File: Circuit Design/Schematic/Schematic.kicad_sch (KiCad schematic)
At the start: 18 parts, among them U1 ESP32-WROOM-32

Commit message: Add files via upload
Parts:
- added Display: Conn_01x04_Female, Connector_PinSocket_2.54mm:PinSocket_1x04_P2.54mm_Vertical, symbol Connector:Conn_01x04_Female
- added Display_: Conn_01x14_Female, Connector_PinSocket_2.54mm:PinSocket_1x14_P2.54mm_Vertical, symbol Connector:Conn_01x14_Female
- added Pull_Down_Miso_Res: 10k, symbol Device:R
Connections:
- net 3v3: now also Display_.14 (Pin_14), Display_.7 (Pin_7)
- net GND: now also Display_.13 (Pin_13), Pull_Down_Miso_Res.2
- net MISO: now also Display_.6 (Pin_6), Pull_Down_Miso_Res.1
- net MOSI: now also Display_.9 (Pin_9)
- net Rst_2: now also U1.12 (IO27); no longer U1.23 (IO15)
- net SCK: now also Display_.8 (Pin_8)
- net IO13: now reaches R_prog.2, U1.16 (IO13)
- net Rst_D: now reaches U1.6 (IO34)
- net Rst_D: now also Display_.11 (Pin_11)
- net D/C: now reaches U1.7 (IO35)
- net D/C: now also Display_.10 (Pin_10)
- new net CS_Display: Display_.12 (Pin_12), U1.23 (IO15)
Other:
- note added: "Display"
- moved on the sheet: J_Motor_1, J_Motor_2, LED_prog, R_prog

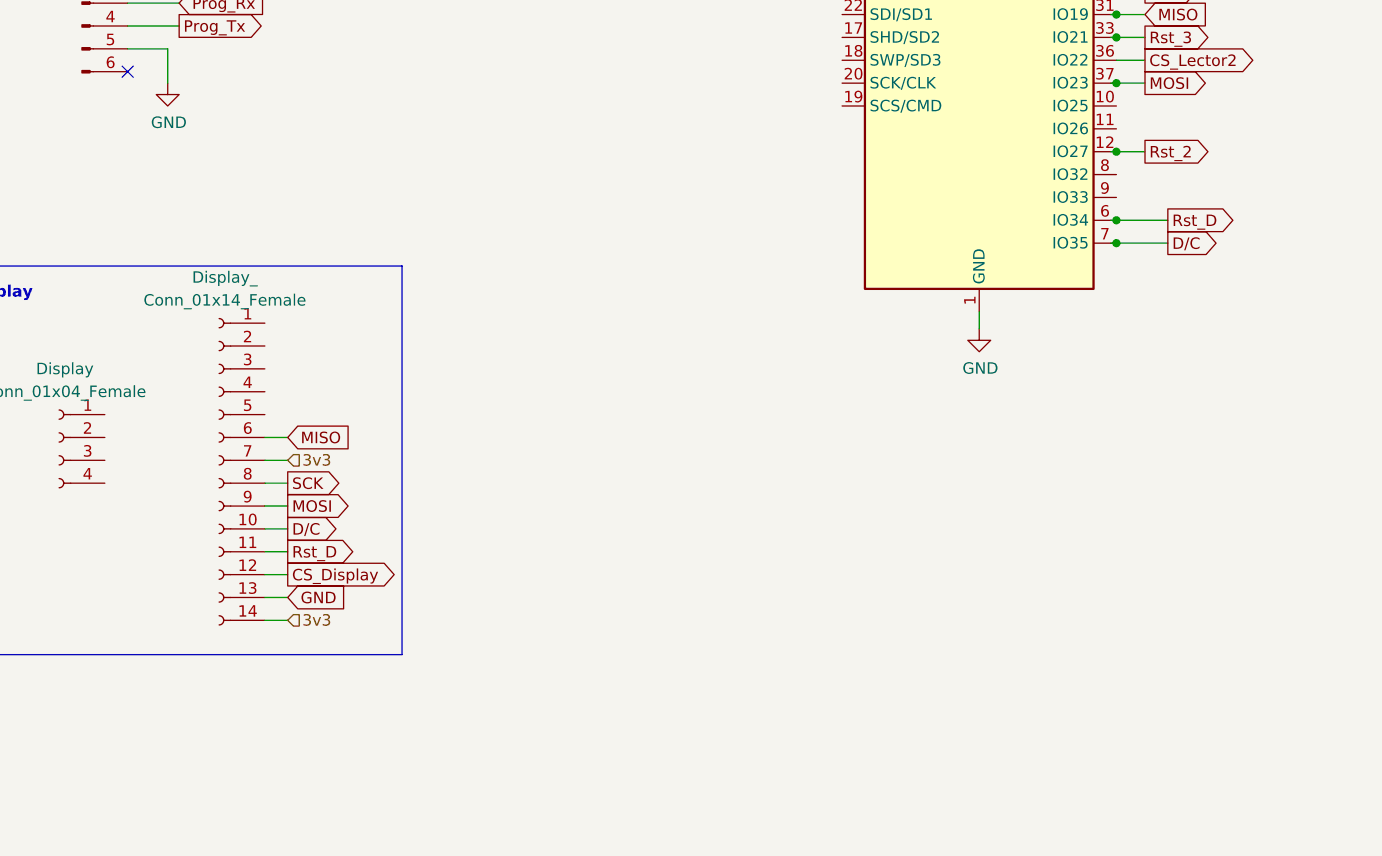
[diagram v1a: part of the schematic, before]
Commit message: I2C interface added
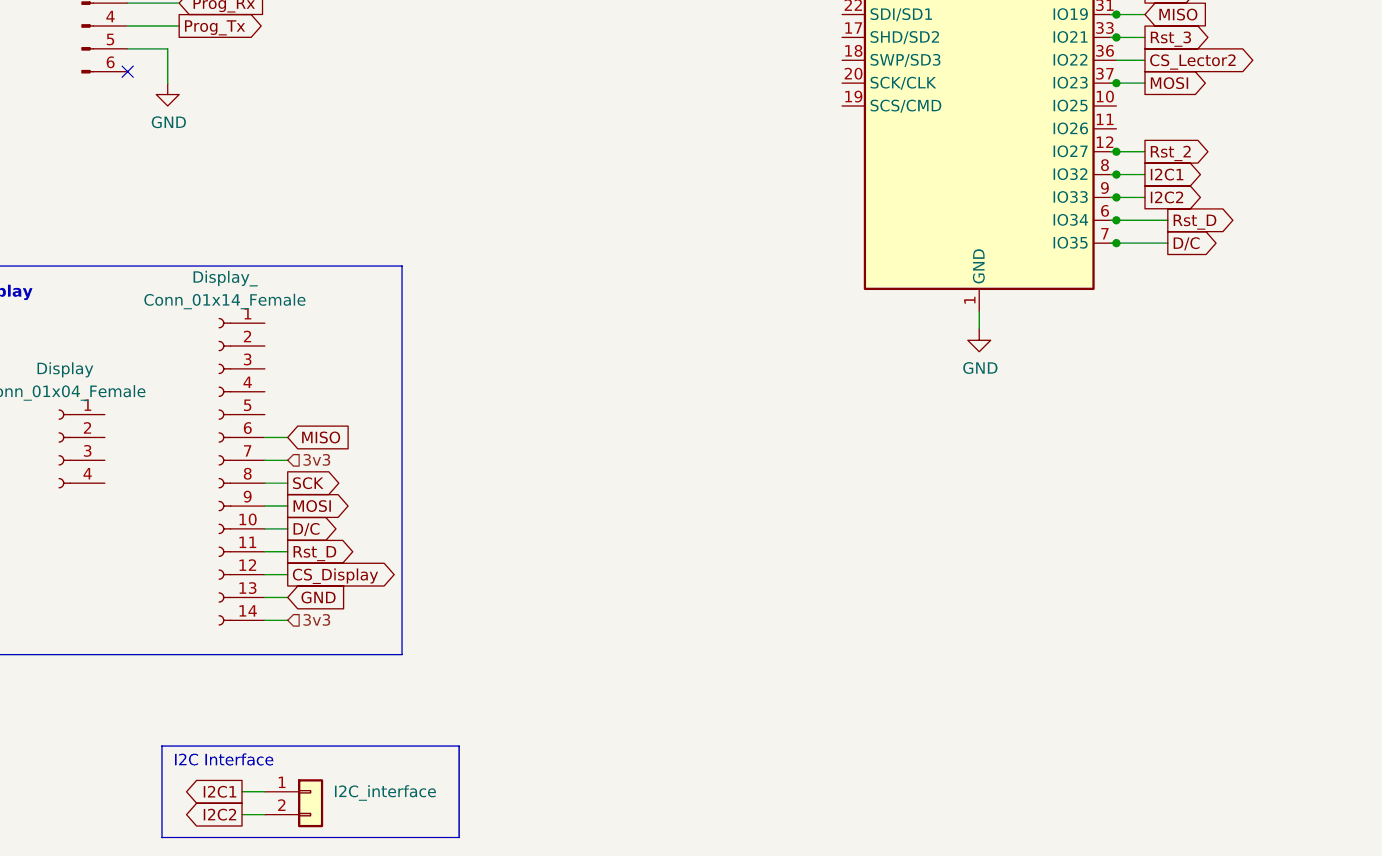
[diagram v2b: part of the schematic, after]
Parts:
- added I2C_interface: (no value), symbol Connector_Generic:Conn_01x02
- Display: footprint Connector_PinSocket_2.54mm:PinSocket_1x04_P2.54mm_Vertical -> (none)
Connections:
- net I2C1: now reaches U1.8 (IO32)
- net I2C1: now also I2C_interface.1 (Pin_1)
- net I2C2: now reaches U1.9 (IO33)
- net I2C2: now also I2C_interface.2 (Pin_2)
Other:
- note added: "I2C Interface"
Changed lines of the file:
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@@
   (junction (at 159.385 77.47) (diameter 0) (color 0 0 0 0)
   )
+  (junction (at 159.385 100.33) (diameter 0) (color 0 0 0 0)
+  )
   (junction (at 159.385 67.31) (diameter 0) (color 0 0 0 0)
   )
@@
   )
   (junction (at 171.45 49.53) (diameter 0) (color 0 0 0 0)
+  )
+  (junction (at 159.385 102.87) (diameter 0) (color 0 0 0 0)
   )
   (junction (at 123.19 49.53) (diameter 0) (color 0 0 0 0)
@@
     (stroke (width 0) (type default) (color 0 0 0 0))
   )
+  (polyline (pts (xy 53.34 163.83) (xy 86.36 163.83))
+    (stroke (width 0) (type default) (color 0 0 0 0))
+  )
   (wire (pts (xy 171.45 31.75) (xy 171.45 49.53))
     (stroke (width 0) (type default) (color 0 0 0 0))
@@
     (stroke (width 0) (type default) (color 0 0 0 0))
   )
+  (polyline (pts (xy 86.36 163.83) (xy 86.36 173.99))
+    (stroke (width 0) (type default) (color 0 0 0 0))
+  )
   (wire (pts (xy 144.78 31.75) (xy 144.78 40.64))
     (stroke (width 0) (type default) (color 0 0 0 0))
@@
     (stroke (width 0) (type default) (color 0 0 0 0))
   )
+  (wire (pts (xy 62.23 171.45) (xy 64.77 171.45))
+    (stroke (width 0) (type default) (color 0 0 0 0))
+  )
   (wire (pts (xy 53.975 90.17) (xy 53.975 86.36))
     (stroke (width 0) (type default) (color 0 0 0 0))
@@
     (stroke (width 0) (type default) (color 0 0 0 0))
   )
+  (wire (pts (xy 158.75 100.33) (xy 159.385 100.33))
+    (stroke (width 0) (type default) (color 0 0 0 0))
+  )
   (wire (pts (xy 204.47 31.75) (xy 204.47 49.53))
     (stroke (width 0) (type default) (color 0 0 0 0))
@@
     (stroke (width 0) (type default) (color 0 0 0 0))
   )
+  (wire (pts (xy 62.23 168.91) (xy 64.77 168.91))
+    (stroke (width 0) (type default) (color 0 0 0 0))
+  )
+  (wire (pts (xy 158.75 102.87) (xy 159.385 102.87))
+    (stroke (width 0) (type default) (color 0 0 0 0))
+  )
   (wire (pts (xy 123.19 31.75) (xy 123.19 49.53))
     (stroke (width 0) (type default) (color 0 0 0 0))
   )
+  (wire (pts (xy 159.385 100.33) (xy 162.56 100.33))
+    (stroke (width 0) (type default) (color 0 0 0 0))
+  )
+  (wire (pts (xy 159.385 102.87) (xy 162.56 102.87))
+    (stroke (width 0) (type default) (color 0 0 0 0))
+  )
   (wire (pts (xy 54.61 38.1) (xy 54.61 36.195))
     (stroke (width 0) (type default) (color 0 0 0 0))
@@
   )
   (wire (pts (xy 54.61 43.18) (xy 54.61 46.355))
+    (stroke (width 0) (type default) (color 0 0 0 0))
+  )
+  (polyline (pts (xy 53.34 163.83) (xy 53.34 173.99))
+    (stroke (width 0) (type default) (color 0 0 0 0))
+  )
+  (polyline (pts (xy 86.36 173.99) (xy 53.34 173.99))
     (stroke (width 0) (type default) (color 0 0 0 0))
   )
@@
     (effects (font (size 1.27 1.27) (thickness 0.254) bold) (justify left bottom))
   )
+  (text "I2C Interface\n" (at 54.61 166.37 0)
+    (effects (font (size 1.27 1.27)) (justify left bottom))
+  )
   (global_label "D{slash}C" (shape output) (at 67.31 139.7 0) (fields_autoplaced)
     (effects (font (size 1.27 1.27)) (justify left))
@@
     )
   )
+  (global_label "I2C1" (shape output) (at 162.56 100.33 0) (fields_autoplaced)
+    (effects (font (size 1.27 1.27)) (justify left))
+    (property "Intersheet References" "${INTERSHEET_REFS}" (id 0) (at 169.178 100.2506 0)
+      (effects (font (size 1.27 1.27)) (justify left) hide)
+    )
+  )
   (global_label "MOSI" (shape output) (at 204.47 96.52 180) (fields_autoplaced)
     (effects (font (size 1.27 1.27)) (justify right))
@@
     )
   )
+  (global_label "I2C2" (shape output) (at 62.23 171.45 180) (fields_autoplaced)
+    (effects (font (size 1.27 1.27)) (justify right))
+    (property "Intersheet References" "${INTERSHEET_REFS}" (id 0) (at 55.612 171.3706 0)
+      (effects (font (size 1.27 1.27)) (justify right) hide)
+    )
+  )
   (global_label "Rst_1" (shape output) (at 162.56 59.69 0) (fields_autoplaced)
     (effects (font (size 1.27 1.27)) (justify left))
@@
     )
   )
+  (global_label "I2C2" (shape output) (at 162.56 102.87 0) (fields_autoplaced)
+    (effects (font (size 1.27 1.27)) (justify left))
+    (property "Intersheet References" "${INTERSHEET_REFS}" (id 0) (at 169.178 102.7906 0)
+      (effects (font (size 1.27 1.27)) (justify left) hide)
+    )
+  )
   (global_label "SCK" (shape output) (at 204.47 146.05 180) (fields_autoplaced)
     (effects (font (size 1.27 1.27)) (justify right))
@@
     (property "Intersheet References" "${INTERSHEET_REFS}" (id 0) (at 169.2385 67.2306 0)
       (effects (font (size 1.27 1.27)) (justify left) hide)
+    )
+  )
+  (global_label "I2C1" (shape output) (at 62.23 168.91 180) (fields_autoplaced)
+    (effects (font (size 1.27 1.27)) (justify right))
+    (property "Intersheet References" "${INTERSHEET_REFS}" (id 0) (at 55.612 168.8306 0)
+      (effects (font (size 1.27 1.27)) (justify right) hide)
     )
   )
@@
     (property "Reference" "Display" (id 0) (at 42.545 121.92 0))
     (property "Value" "Conn_01x04_Female" (id 1) (at 42.545 124.46 0))
-    (property "Footprint" "Connector_PinSocket_2.54mm:PinSocket_1x04_P2.54mm_Vertical" (id 2) (at 41.91 129.54 0)
+    (property "Footprint" "" (id 2) (at 41.91 129.54 0)
       (effects (font (size 1.27 1.27)) hide)
     )
@@
     (pin "3")
     (pin "4")
+  )
+  (symbol (lib_id "Connector_Generic:Conn_01x02") (at 69.85 168.91 0) (unit 1)
+    (in_bom yes) (on_board yes) (fields_autoplaced)
+    (property "Reference" "I2C_interface" (id 0) (at 72.39 168.9099 0)
+      (effects (font (size 1.27 1.27)) (justify left))
+    )
+    (property "Value" "" (id 1) (at 72.39 171.4499 0)
+      (effects (font (size 1.27 1.27)) (justify left))
+    )
+    (property "Footprint" "" (id 2) (at 69.85 168.91 0)
+      (effects (font (size 1.27 1.27)) hide)
+    )
+    (property "Datasheet" "~" (id 3) (at 69.85 168.91 0)
+      (effects (font (size 1.27 1.27)) hide)
+    )
+    (pin "1")
+    (pin "2")
   )
   (symbol (lib_id "power:GND") (at 250.19 121.92 0) (unit 1)
@@
       (reference "ESP_Reset") (unit 1) (value "SW_DIP_x01") (footprint "")
     )
+    (path "/567b521c-82db-4d61-8d43-df73e3cabec5"
+      (reference "I2C_interface") (unit 1) (value "Conn_01x02") (footprint "Connector_PinSocket_2.54mm:PinSocket_1x02_P2.54mm_Vertical")
+    )
     (path "/a45a8d32-ecf4-4f16-b72c-3f69eaa16341"

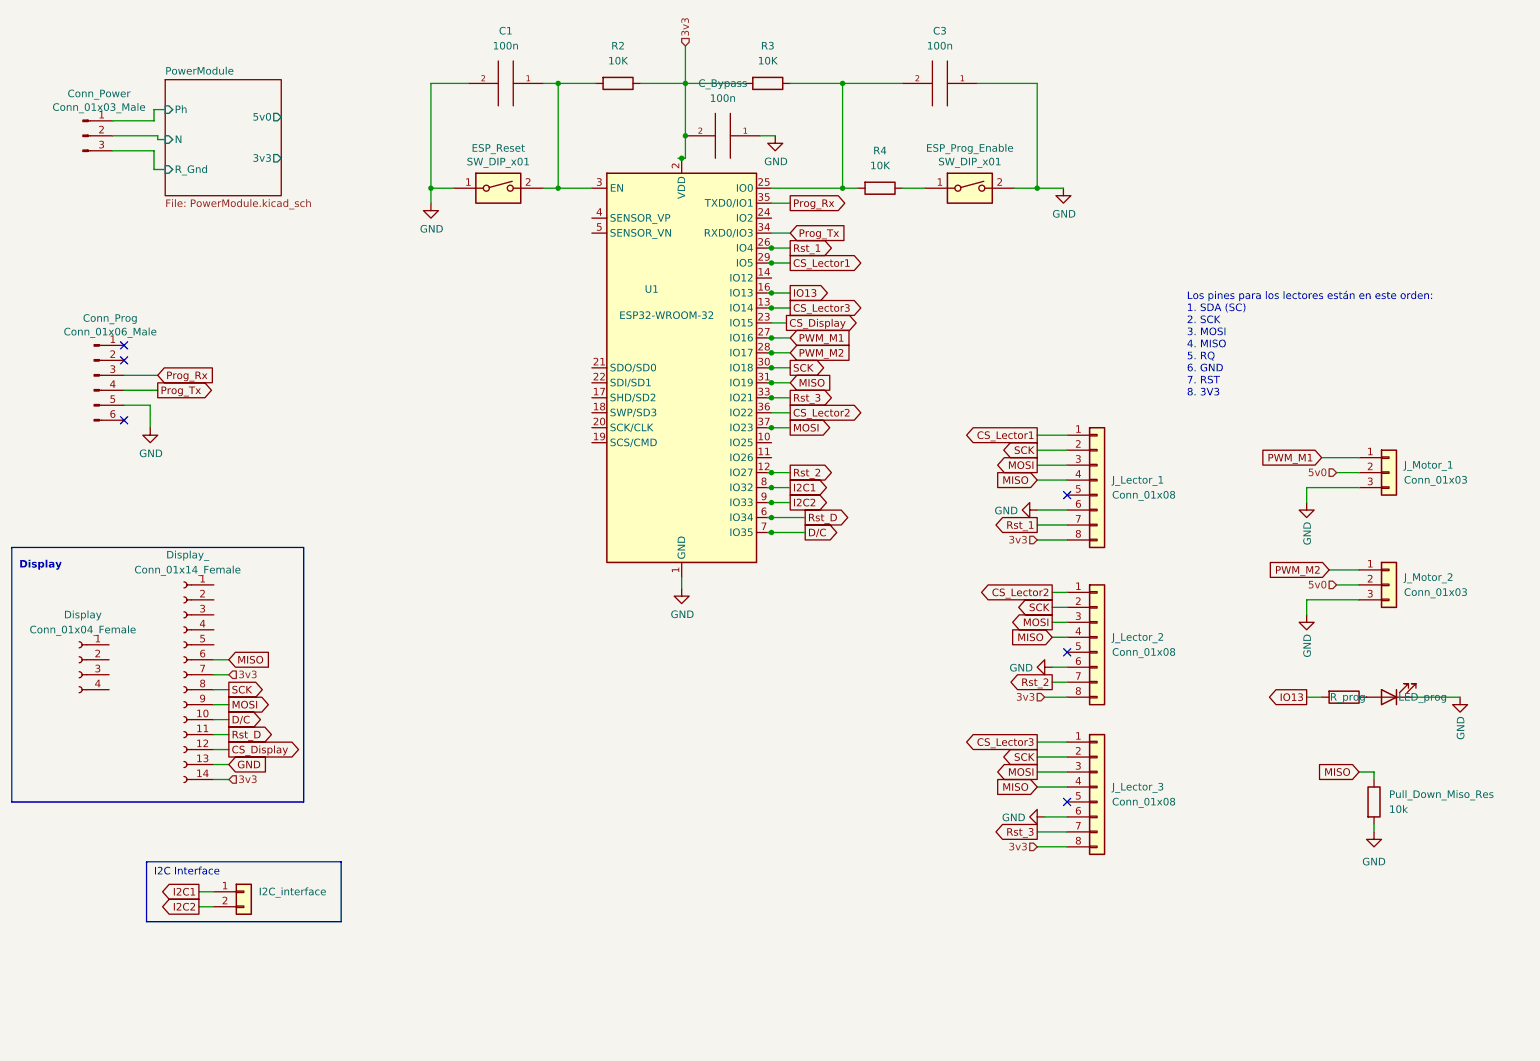
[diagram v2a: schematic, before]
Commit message: Botones de reporte
Se agregan los botones de reporte y se determinan los puertos que no serán utilizados
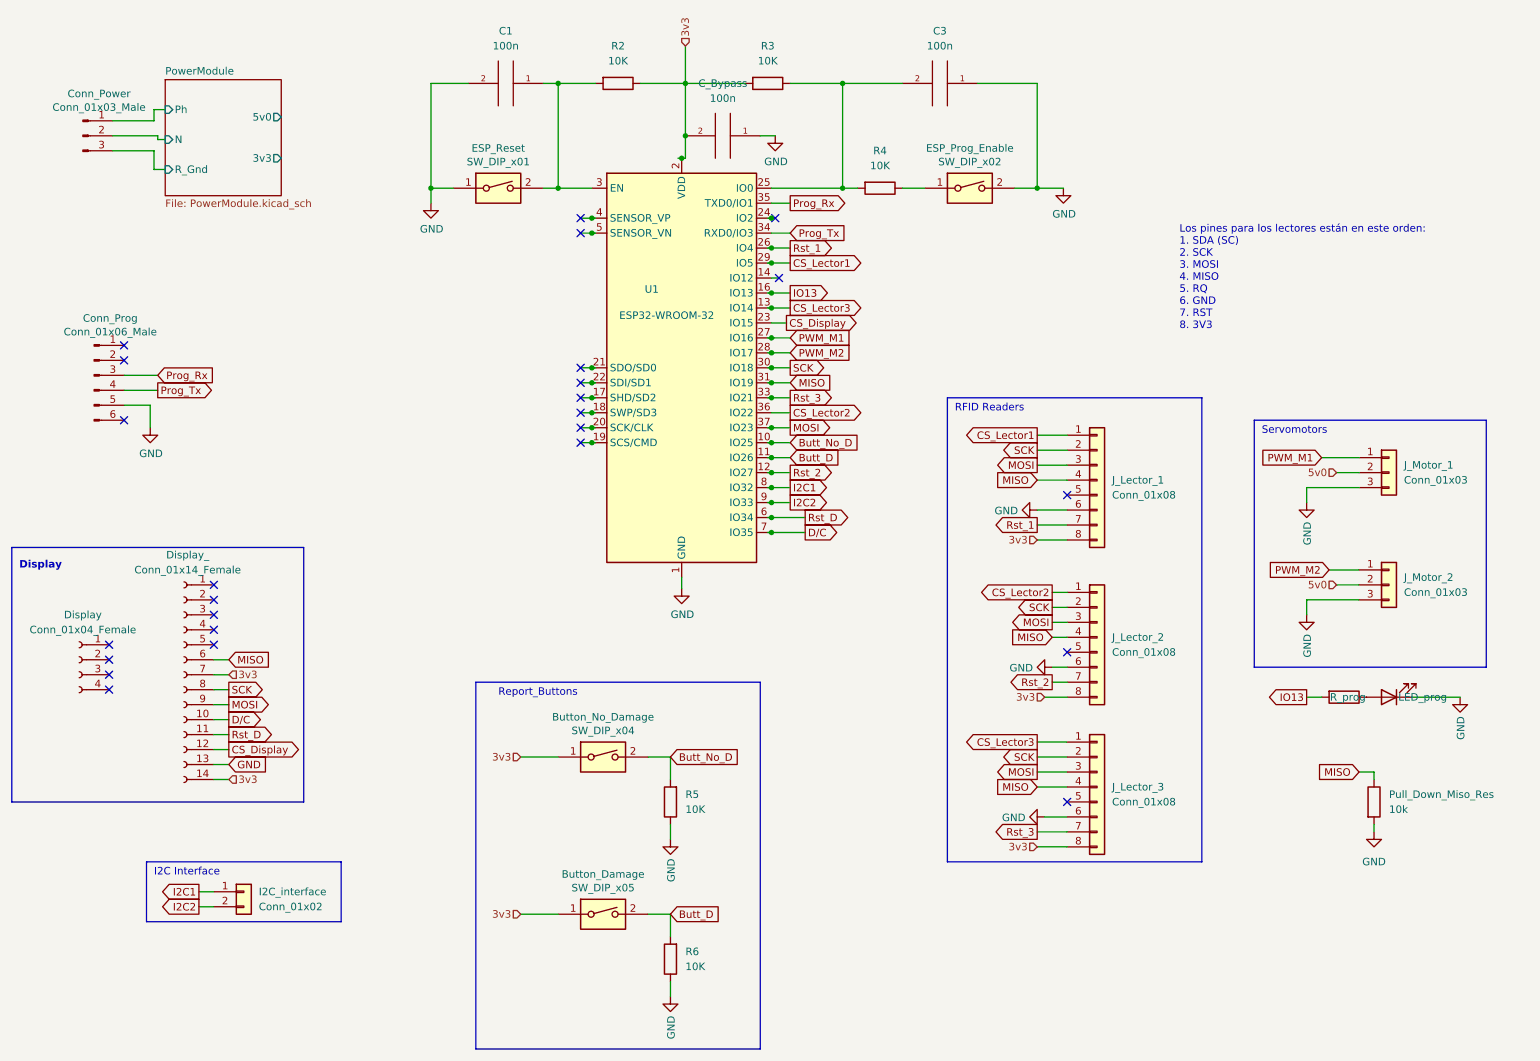
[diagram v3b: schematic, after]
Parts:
- added Button_Damage: SW_DIP_x05, symbol Switch:SW_DIP_x01
- added Button_No_Damage: SW_DIP_x04, symbol Switch:SW_DIP_x01
- added R5, R6: 10K, symbol Device:R
- Display: footprint (none) -> Connector_PinSocket_2.54mm:PinSocket_1x04_P2.54mm_Vertical
- ESP_Prog_Enable: value SW_DIP_x01 -> SW_DIP_x02
- I2C_interface: value (none) -> Conn_01x02; footprint (none) -> Connector_PinSocket_2.54mm:PinSocket_1x02_P2.54mm_Vertical
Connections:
- net 3v3: now also Button_Damage.1, Button_No_Damage.1
- net GND: now also R5.1, R6.1
- net Butt_No_D: now reaches U1.10 (IO25)
- net Butt_No_D: now also Button_No_Damage.2, R5.2
- net Butt_D: now reaches U1.11 (IO26)
- net Butt_D: now also Button_Damage.2, R6.2
- no-connect marks 6 -> 25
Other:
- note added: "RFID Readers"
- note added: "Report_Buttons"
- note added: "Servomotors"
